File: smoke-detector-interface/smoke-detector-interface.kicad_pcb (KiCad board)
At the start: 2 copper layers, 55.9 x 106.7 mm, 46 parts, among them J1 Conn_01x04_Pin, J2 M50-3500542, J3 DE9_Receptacle, J4 61200621621, J5 Conn_01x06_Pin, U2 AS7805AT, U3 ATtiny13A-P, U6 TL072

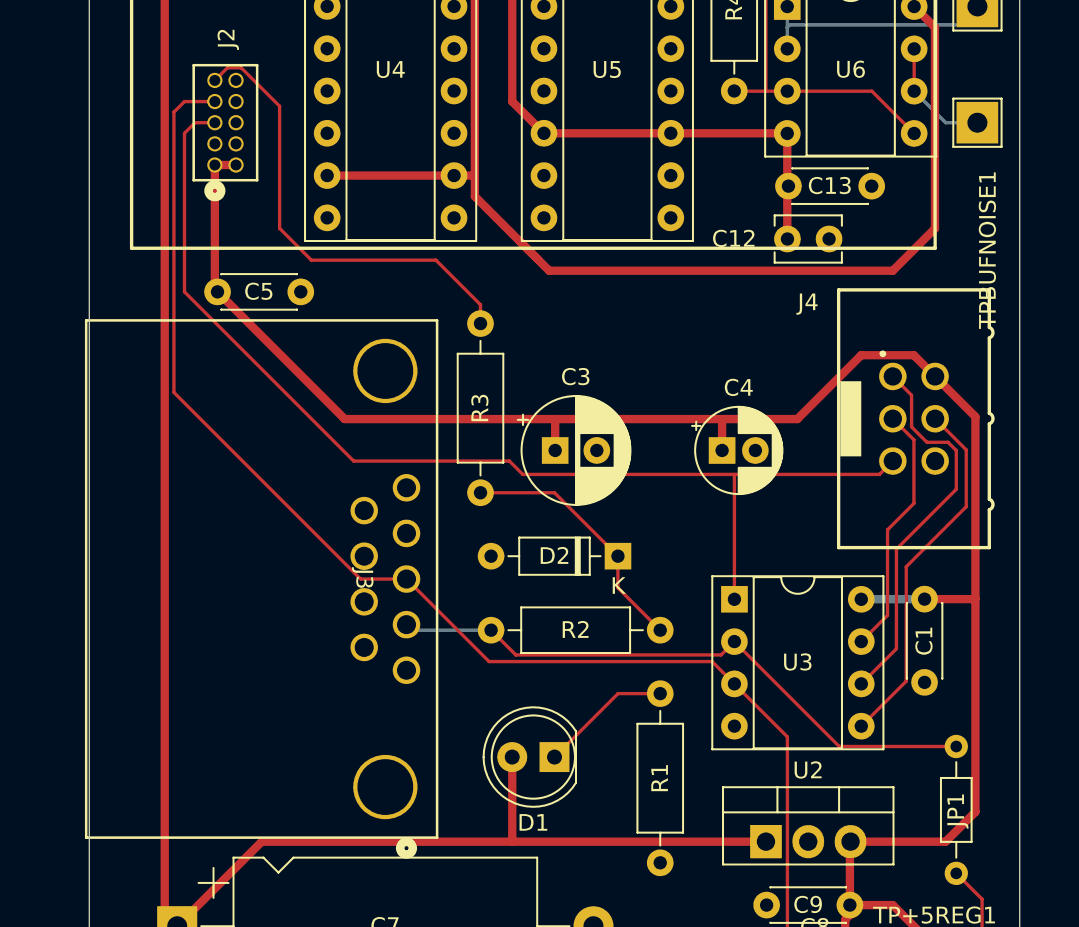
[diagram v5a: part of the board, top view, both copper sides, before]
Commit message: Add jumpers to serial rx/tx in case they need swapping.
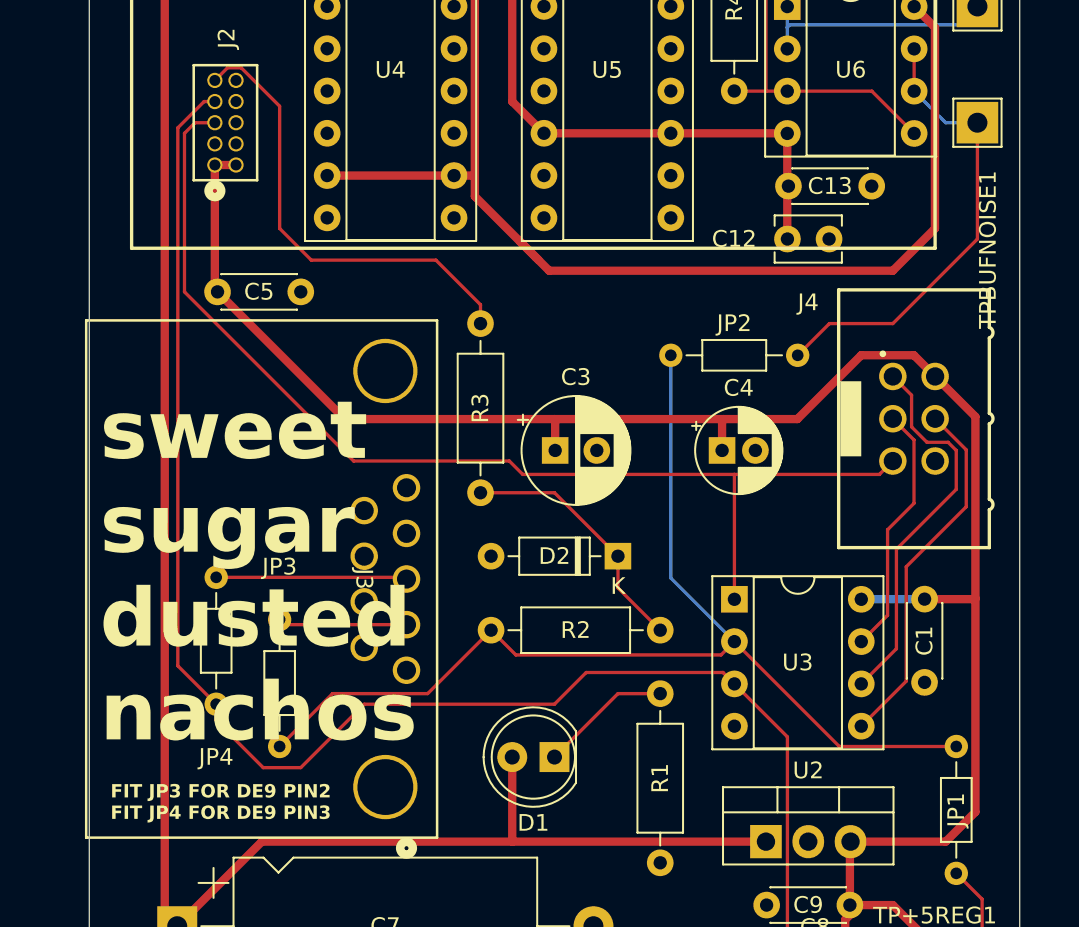
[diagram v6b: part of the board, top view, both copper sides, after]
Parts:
- added JP2: Jumper_2_Open, Resistor_THT:R_Axial_DIN0204_L3.6mm_D1.6mm_P7.62mm_Horizontal, F.Cu at (132.7, 104.1)
- added JP3: Jumper_2_Open, Resistor_THT:R_Axial_DIN0204_L3.6mm_D1.6mm_P7.62mm_Horizontal, F.Cu at (109.2, 120.0)
- added JP4: Jumper_2_Open, Resistor_THT:R_Axial_DIN0204_L3.6mm_D1.6mm_P7.62mm_Horizontal, F.Cu at (105.4, 117.5)
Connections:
- net Net-(U6B--) renamed BUFFERED_NOISE
- J3 pad 2: HOSTTX -> Net-(JP3-A)
- J3 pad 3: HOSTRX -> Net-(JP4-A)
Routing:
- net HOSTTX: track 36.7 -> 65.9 mm
- net BUFFERED_NOISE: track 7.12 -> 27.8 mm
- net HOSTRX: track 93.2 -> 107.1 mm
- net Net-(JP4-A): track 0.00 -> 11.5 mm
- net Net-(JP3-A): track 0.00 -> 7.74 mm
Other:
- board text added: "FIT JP3 FOR DE9 PIN2 FIT JP4 FOR DE9 PIN3"
- board text added: "sweet sugar dusted nachos"

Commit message: First production candidate.
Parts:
- added F1: Fuse, ThirdPartyFootprints:01530008, F.Cu at (138.4, 148.8)
- added TP12VIN1: +12, TestPoint:TestPoint_THTPad_2.5x2.5mm_Drill1.2mm, F.Cu at (132.1, 142.2)
- moved JP2 9.53 mm to (132.7, 113.7), turned to 90 degrees
- moved C8 0.64 mm to (143.2, 141.6)
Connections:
- J1 pad 1: +12V -> Net-(J1-Pin_1)
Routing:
- net Net-(J1-Pin_1): track 0.00 -> 31.6 mm
- net +12V: track 183.1 -> 156.2 mm
- net HOSTTX: track 65.9 -> 56.3 mm
- net BUFFERED_NOISE: track 27.8 -> 35.5 mm
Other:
- rule pad_to_mask_clearance: 0 -> 0.038
- board text added: "TX RX GND (POLULU)"
